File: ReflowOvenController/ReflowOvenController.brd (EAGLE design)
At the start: 75.9 x 54.3 mm, 33 parts, among them IC1 IC_OP-AMP_LM358-SO8, SW2 EC12E_SW, U1 UA78L05CPK

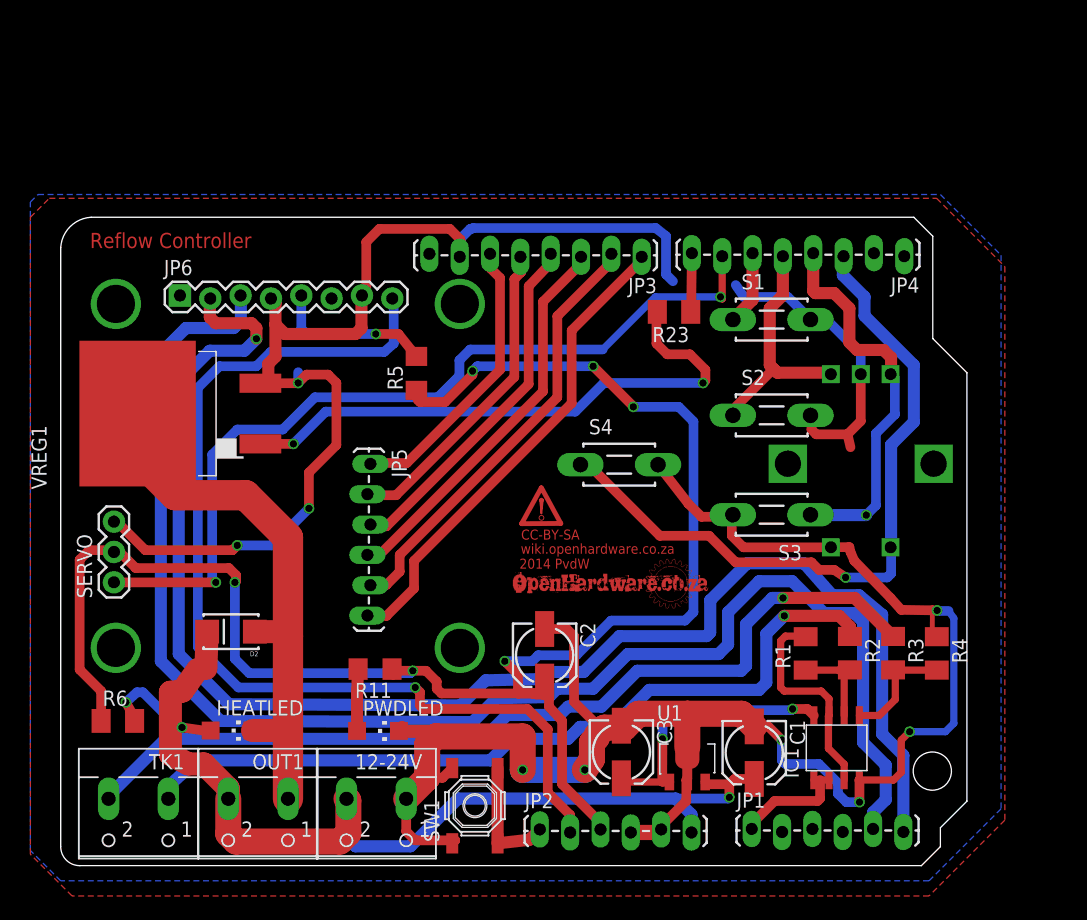
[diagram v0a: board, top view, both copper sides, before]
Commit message: Tiny-TinyG, Plus gerbers of Reflow and Advertisement
Started new project: TinyTinyG
Generated Gerbers for Advertisement Display driver and ReflowOvenShield
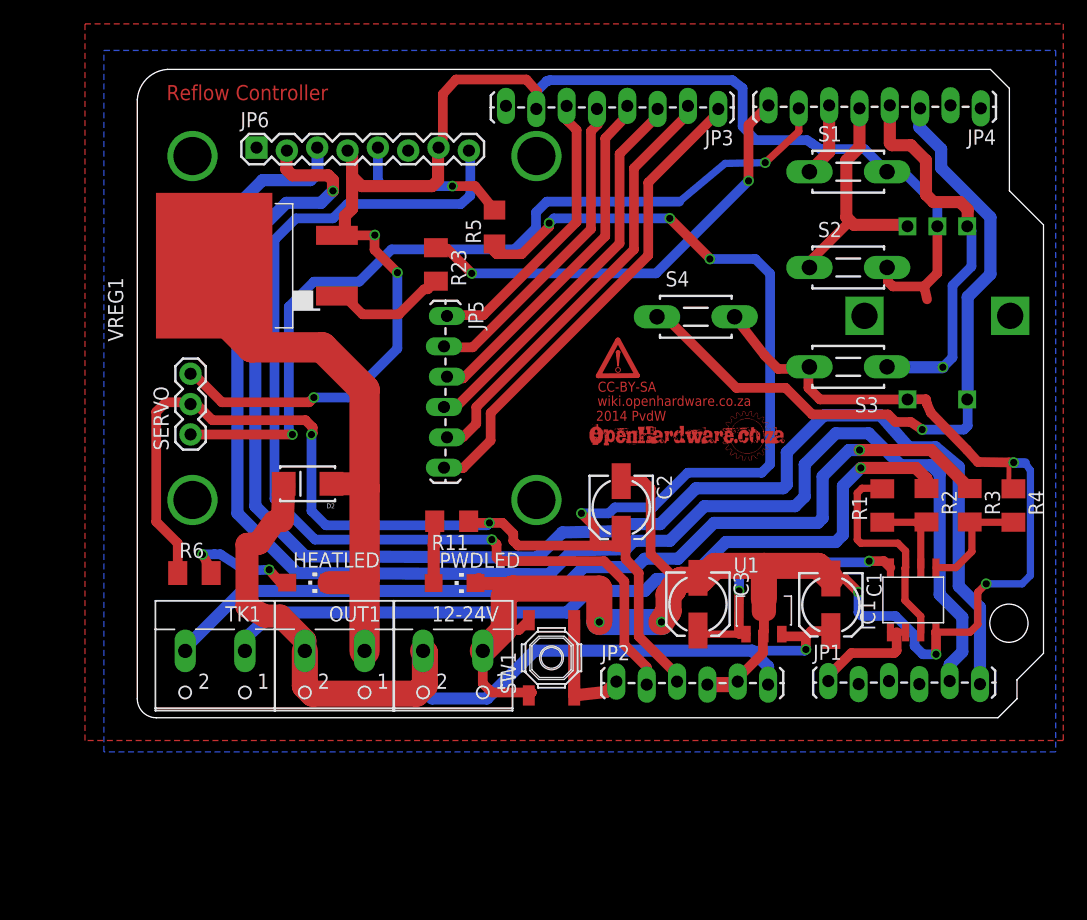
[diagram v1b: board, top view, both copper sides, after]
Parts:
- moved R23 20.3 mm to (51.6, -8.71), turned to 270 degrees
- moved R1 13.9 mm to (89.0, -28.9)
- moved JP6 13.9 mm to (36.6, 0.94)
- moved R2 13.9 mm to (92.7, -28.9)
- moved R3 13.9 mm to (96.3, -28.9)
- moved TK1 13.9 mm to (33.1, -42.3)
- moved JP5 13.9 mm to (52.5, -13.0)
- moved S2 13.9 mm to (86.1, -8.97)
- moved 12-24V 13.9 mm to (53.0, -42.3)
- moved C1 13.9 mm to (84.7, -37.2)
- moved C3 13.9 mm to (73.6, -37.2)
- moved D2 13.9 mm to (40.9, -27.1)
- moved HEATLED 13.9 mm to (40.9, -35.4)
- moved IC1 13.9 mm to (91.6, -36.8)
- moved JP1 13.9 mm to (84.5, -43.6)
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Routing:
- net N$43: track 48.1 -> 10.1 mm, vias 2 -> 0
- net D7: track 4.93 -> 37.3 mm, vias 0 -> 2
- net D6: track 71.9 -> 70.6 mm
- net GND: track 275.3 -> 276.3 mm
- net N$4: track 10.4 -> 9.82 mm
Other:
- board text added: "[BACK]"
